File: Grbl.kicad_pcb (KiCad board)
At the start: 2 copper layers, 68.5 x 56.6 mm, 22 parts, among them P1 CTL, P2 MISC, P3 STEP, P4 SPIN, P5 LIMIT, P6 GND, P7 GND

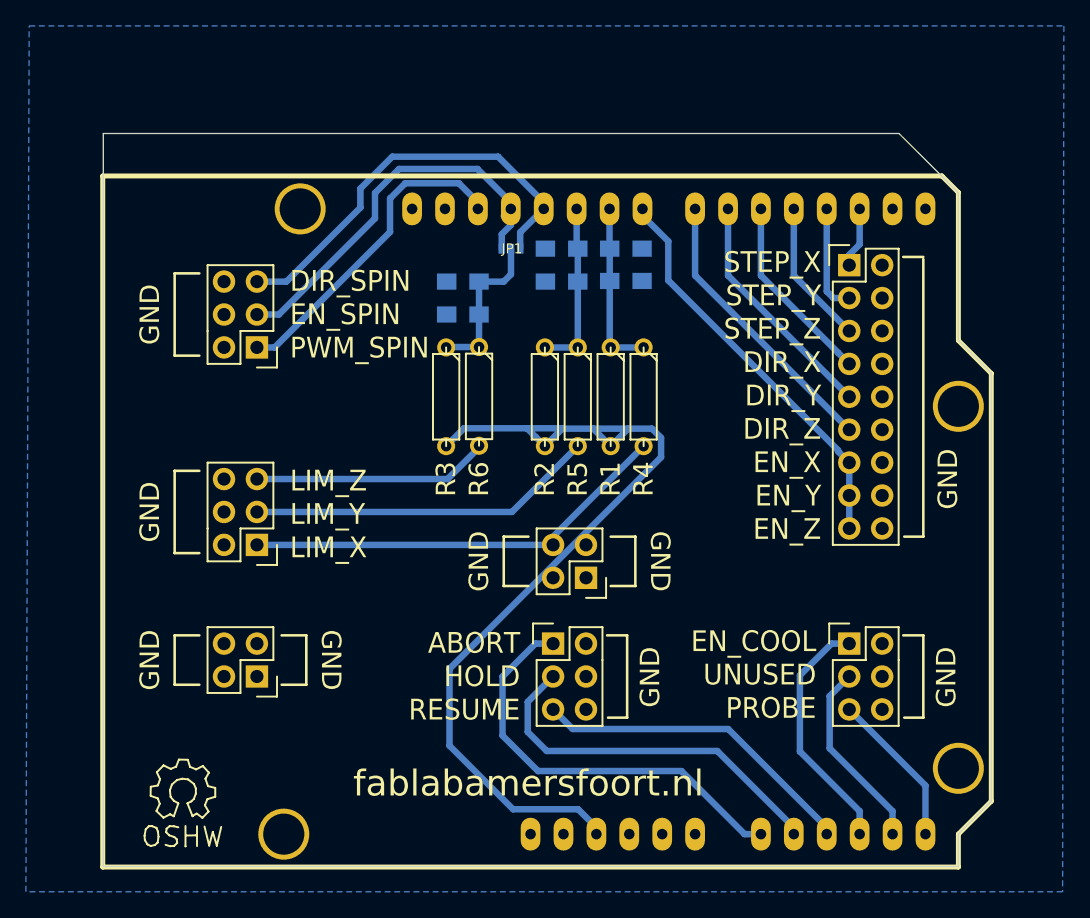
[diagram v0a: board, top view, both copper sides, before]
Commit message: Add a groundplane on the front
This adds a filled zone and some vias.
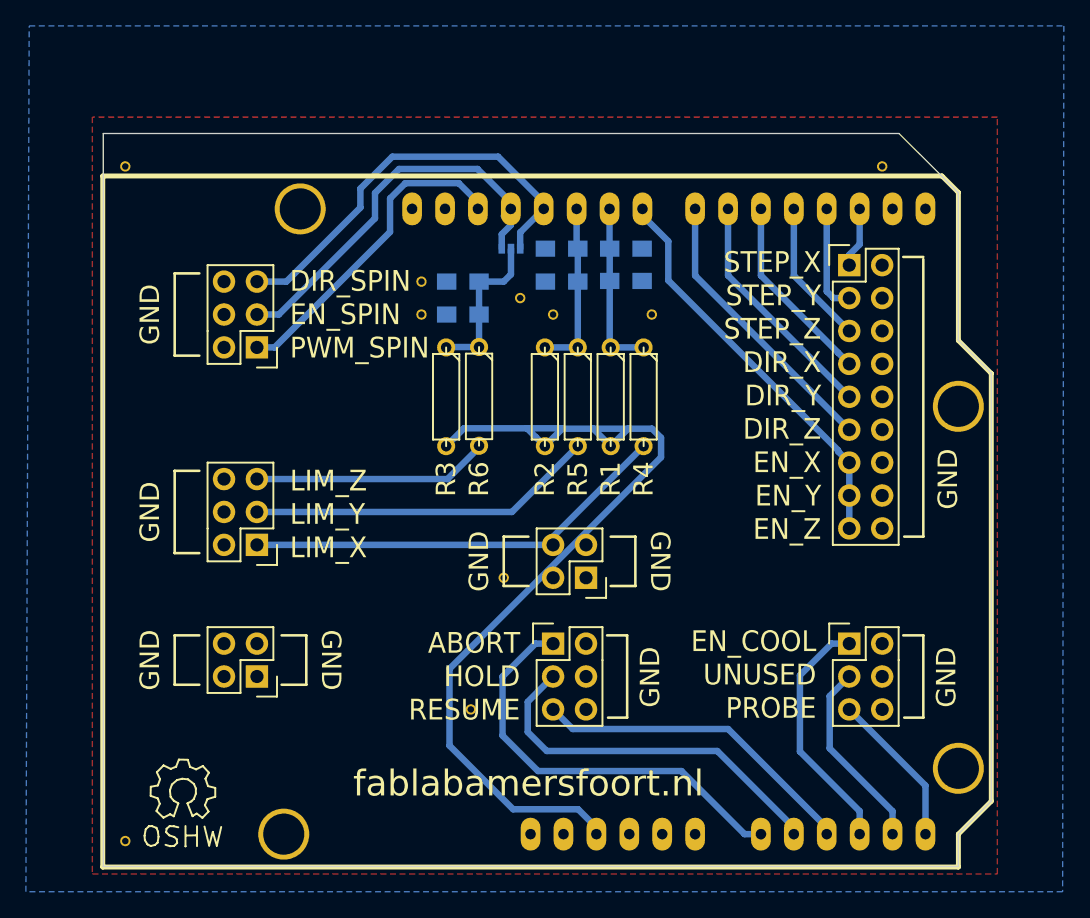
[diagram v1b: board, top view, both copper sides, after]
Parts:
- added REF**: via0.8size0.5drill, Footprints:stitching_via, F.Cu at (172.7, 78.7)
- added REF**: via0.8size0.5drill, Footprints:stitching_via, F.Cu at (179.1, 101.6)
- added REF**: via0.8size0.5drill, Footprints:stitching_via, F.Cu at (172.7, 81.3)
- added REF**: via0.8size0.5drill, Footprints:stitching_via, F.Cu at (180.3, 80.0)
- added REF**: via0.8size0.5drill, Footprints:stitching_via, F.Cu at (182.9, 81.3)
- added REF**: via0.8size0.5drill, Footprints:stitching_via, F.Cu at (190.5, 81.3)
- added REF**: via0.8size0.5drill, Footprints:stitching_via, F.Cu at (208.3, 69.8)
- added REF**: via0.8size0.5drill, Footprints:stitching_via, F.Cu at (149.9, 69.8)
- added REF**: via0.8size0.5drill, Footprints:stitching_via, F.Cu at (149.9, 121.9)
- added REF**: via0.8size0.5drill, Footprints:stitching_via, F.Cu at (176.5, 111.8)
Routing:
- added copper zone on F.Cu, net GND
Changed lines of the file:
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@@
 (kicad_pcb (version 4) (host pcbnew 4.0.6-e0-6349~53~ubuntu16.04.1)
   (general
-    (links 75)
-    (no_connects 4)
-    (area 148.109619 67.258053 216.74991 123.932974)
+    (links 84)
+    (no_connects 9)
+    (area 142.1892 59.0042 222.300801 125.94582)
     (thickness 1.6)
     (drawings 52)
     (tracks 129)
     (zones 0)
-    (modules 22)
+    (modules 32)
     (nets 31)
   )
@@
     (mod_text_size 1 1)
     (mod_text_width 0.15)
-    (pad_size 3.937 3.937)
-    (pad_drill 3.175)
+    (pad_size 0.8 0.8)
+    (pad_drill 0.5)
     (pad_to_mask_clearance 0)
     (aux_axis_origin 147.955 67.31)
@@
     (add_net "Net-(SHIELD1-PadRST)")
     (add_net "Net-(SHIELD1-PadV_IN)")
+  )
+  (module Footprints:stitching_via (layer F.Cu)
+    (at 172.72 78.74)
+    (fp_text reference REF** (at 0 -0.508) (layer F.SilkS) hide
+      (effects (font (size 0.127 0.127) (thickness 0.03175)))
+    )
+    (fp_text value via0.8size0.5drill (at 0 -0.762) (layer F.Fab) hide
+      (effects (font (size 0.127 0.127) (thickness 0.03175)))
+    )
+    (pad "" thru_hole circle (at 0 0) (size 0.8 0.8) (drill 0.5) (layers *.Cu)
+      (net 2 GND) (zone_connect 2))
+  )
+  (module Footprints:stitching_via (layer F.Cu)
+    (at 172.72 81.28)
+    (fp_text reference REF** (at 0 -0.508) (layer F.SilkS) hide
+      (effects (font (size 0.127 0.127) (thickness 0.03175)))
+    )
+    (fp_text value via0.8size0.5drill (at 0 -0.762) (layer F.Fab) hide
+      (effects (font (size 0.127 0.127) (thickness 0.03175)))
+    )
+    (pad "" thru_hole circle (at 0 0) (size 0.8 0.8) (drill 0.5) (layers *.Cu)
+      (net 2 GND) (zone_connect 2))
+  )
+  (module Footprints:stitching_via (layer F.Cu)
+    (at 180.34 80.01)
+    (fp_text reference REF** (at 0 -0.508) (layer F.SilkS) hide
+      (effects (font (size 0.127 0.127) (thickness 0.03175)))
+    )
+    (fp_text value via0.8size0.5drill (at 0 -0.762) (layer F.Fab) hide
+      (effects (font (size 0.127 0.127) (thickness 0.03175)))
+    )
+    (pad "" thru_hole circle (at 0 0) (size 0.8 0.8) (drill 0.5) (layers *.Cu)
+      (net 2 GND) (zone_connect 2))
+  )
+  (module Footprints:stitching_via (layer F.Cu)
+    (at 182.88 81.28)
+    (fp_text reference REF** (at 0 -0.508) (layer F.SilkS) hide
+      (effects (font (size 0.127 0.127) (thickness 0.03175)))
+    )
+    (fp_text value via0.8size0.5drill (at 0 -0.762) (layer F.Fab) hide
+      (effects (font (size 0.127 0.127) (thickness 0.03175)))
+    )
+    (pad "" thru_hole circle (at 0 0) (size 0.8 0.8) (drill 0.5) (layers *.Cu)
+      (net 2 GND) (zone_connect 2))
+  )
+  (module Footprints:stitching_via (layer F.Cu)
+    (at 190.5 81.28)
+    (fp_text reference REF** (at 0 -0.508) (layer F.SilkS) hide
+      (effects (font (size 0.127 0.127) (thickness 0.03175)))
+    )
+    (fp_text value via0.8size0.5drill (at 0 -0.762) (layer F.Fab) hide
+      (effects (font (size 0.127 0.127) (thickness 0.03175)))
+    )
+    (pad "" thru_hole circle (at 0 0) (size 0.8 0.8) (drill 0.5) (layers *.Cu)
+      (net 2 GND) (zone_connect 2))
+  )
+  (module Footprints:stitching_via (layer F.Cu)
+    (at 208.28 69.85)
+    (fp_text reference REF** (at 0 -0.508) (layer F.SilkS) hide
+      (effects (font (size 0.127 0.127) (thickness 0.03175)))
+    )
+    (fp_text value via0.8size0.5drill (at 0 -0.762) (layer F.Fab) hide
+      (effects (font (size 0.127 0.127) (thickness 0.03175)))
+    )
+    (pad "" thru_hole circle (at 0 0) (size 0.8 0.8) (drill 0.5) (layers *.Cu)
+      (net 2 GND) (zone_connect 2))
+  )
+  (module Footprints:stitching_via (layer F.Cu)
+    (at 149.86 69.85)
+    (fp_text reference REF** (at 0 -0.508) (layer F.SilkS) hide
+      (effects (font (size 0.127 0.127) (thickness 0.03175)))
+    )
+    (fp_text value via0.8size0.5drill (at 0 -0.762) (layer F.Fab) hide
+      (effects (font (size 0.127 0.127) (thickness 0.03175)))
+    )
+    (pad "" thru_hole circle (at 0 0) (size 0.8 0.8) (drill 0.5) (layers *.Cu)
+      (net 2 GND) (zone_connect 2))
+  )
+  (module Footprints:stitching_via (layer F.Cu)
+    (at 149.86 121.92)
+    (fp_text reference REF** (at 0 -0.508) (layer F.SilkS) hide
+      (effects (font (size 0.127 0.127) (thickness 0.03175)))
+    )
+    (fp_text value via0.8size0.5drill (at 0 -0.762) (layer F.Fab) hide
+      (effects (font (size 0.127 0.127) (thickness 0.03175)))
+    )
+    (pad "" thru_hole circle (at 0 0) (size 0.8 0.8) (drill 0.5) (layers *.Cu)
+      (net 2 GND) (zone_connect 2))
+  )
+  (module Footprints:stitching_via (layer F.Cu)
+    (at 176.53 111.76)
+    (fp_text reference REF** (at 0 -0.508) (layer F.SilkS) hide
+      (effects (font (size 0.127 0.127) (thickness 0.03175)))
+    )
+    (fp_text value via0.8size0.5drill (at 0 -0.762) (layer F.Fab) hide
+      (effects (font (size 0.127 0.127) (thickness 0.03175)))
+    )
+    (pad "" thru_hole circle (at 0 0) (size 0.8 0.8) (drill 0.5) (layers *.Cu)
+      (net 2 GND) (zone_connect 2))
   )
   (module Pin_Headers:Pin_Header_Straight_2x02 (layer F.Cu)
@@
     (at 179.6288 76.2 180)
     (descr "Taken from https://github.com/open-project/kicadlibrary")
-    (fp_text reference JP1 (at -0.0762 0 180) (layer F.SilkS)
+    (fp_text reference JP1 (at -0.0762 0 180) (layer F.SilkS) hide
       (effects (font (size 0.762 0.762) (thickness 0.127)))
     )
@@
       (rotate (xyz 0 0 90))
     )
+  )
+  (module Footprints:stitching_via (layer F.Cu)
+    (at 179.07 101.6)
+    (fp_text reference REF** (at 0 -0.508) (layer F.SilkS) hide
+      (effects (font (size 0.127 0.127) (thickness 0.03175)))
+    )
+    (fp_text value via0.8size0.5drill (at 0 -0.762) (layer F.Fab) hide
+      (effects (font (size 0.127 0.127) (thickness 0.03175)))
+    )
+    (pad "" thru_hole circle (at 0 0) (size 0.8 0.8) (drill 0.5) (layers *.Cu)
+      (net 2 GND) (zone_connect 2))
   )
   (gr_line (start 163.83 106.045) (end 163.83 109.855) (layer F.SilkS) (width 0.2))
@@
       )
     )
+  )
+  (zone (net 2) (net_name GND) (layer F.Cu) (hatch edge 0.508)
+    (connect_pads (clearance 0.508))
+    (min_thickness 0.254)
+    (fill yes (arc_segments 16) (thermal_gap 0.508) (thermal_bridge_width 0.508))
+    (polygon
+      (pts
+        (xy 147.32 66.04) (xy 147.32 124.46) (xy 217.17 124.46) (xy 217.17 66.04)
+      )
+    )

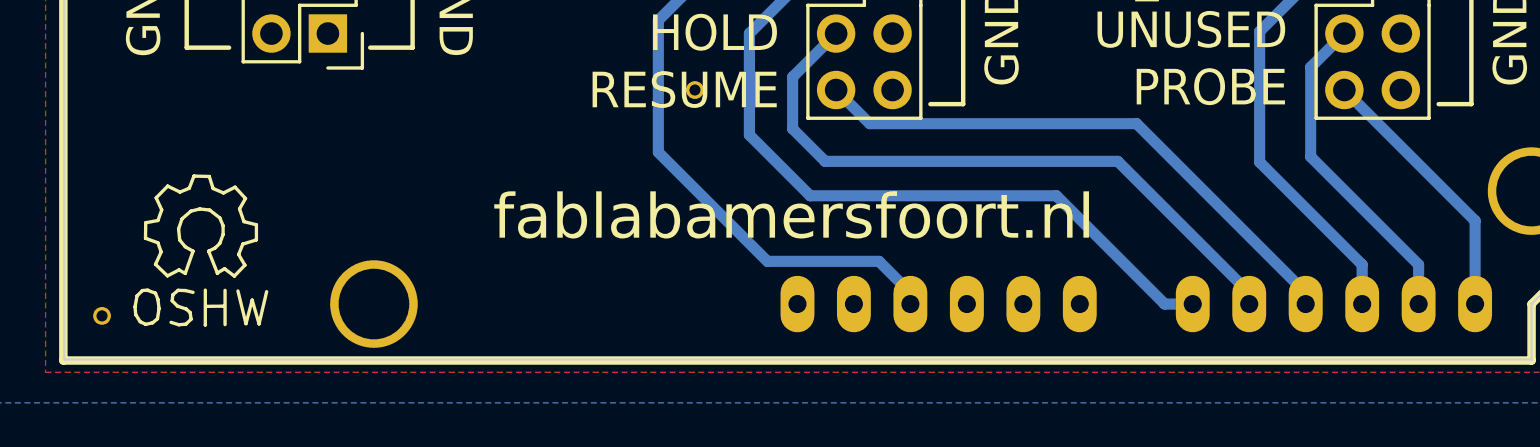
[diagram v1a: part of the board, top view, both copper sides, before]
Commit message: Add "GRBL shield v2" to the silkscreen
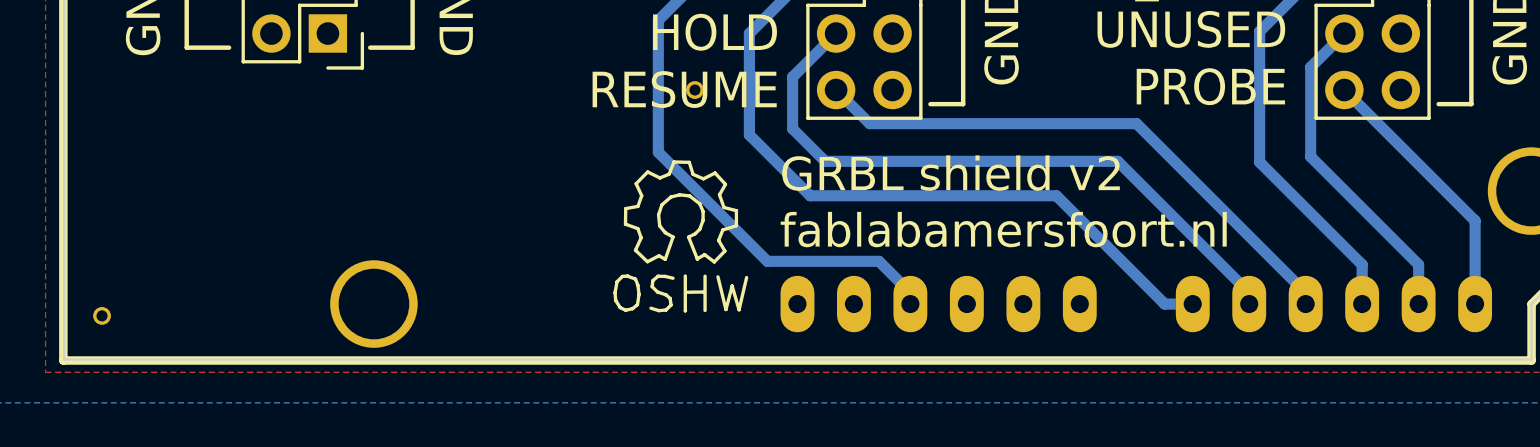
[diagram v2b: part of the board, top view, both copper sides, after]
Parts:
- moved REF** 21.6 mm to (175.9, 117.5)
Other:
- board text added: "GRBL shield v2"
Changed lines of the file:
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@@
     (links 84)
     (no_connects 9)
-    (area 142.1892 59.0042 222.300801 125.94582)
+    (area 148.109619 67.258053 216.74991 123.932974)
     (thickness 1.6)
-    (drawings 52)
+    (drawings 53)
     (tracks 129)
     (zones 0)
@@
     (mod_text_size 1 1)
     (mod_text_width 0.15)
-    (pad_size 0.8 0.8)
-    (pad_drill 0.5)
+    (pad_size 3.937 3.937)
+    (pad_drill 3.175)
     (pad_to_mask_clearance 0)
     (aux_axis_origin 147.955 67.31)
@@
   )
   (module Symbols:Symbol_OSHW-Logo_SilkScreen (layer F.Cu)
-    (at 154.305 118.11)
+    (at 175.895 117.475)
     (descr "Symbol, OSHW-Logo, Silk Screen,")
     (tags "Symbol, OSHW-Logo, Silk Screen,")
@@
       (net 2 GND) (zone_connect 2))
   )
+  (gr_text "GRBL shield v2" (at 180.34 115.57) (layer F.SilkS)
+    (effects (font (size 1.5 1.5) (thickness 0.3)) (justify left))
+  )
   (gr_line (start 163.83 106.045) (end 163.83 109.855) (layer F.SilkS) (width 0.2))
   (gr_text GND (at 165.735 107.95 270) (layer F.SilkS)
@@
     (effects (font (size 1.5 1.5) (thickness 0.3)))
   )
-  (gr_text fablabamersfoort.nl (at 180.975 117.475) (layer F.SilkS)
-    (effects (font (size 2 2) (thickness 0.3)))
+  (gr_text fablabamersfoort.nl (at 180.34 118.11) (layer F.SilkS)
+    (effects (font (size 1.5 1.5) (thickness 0.3)) (justify left))
   )
   (gr_text "R1-R3: pullups\nR4-R6: filter" (at 193.04 81.28 270) (layer F.Fab)
